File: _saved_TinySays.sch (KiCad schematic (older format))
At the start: 31 parts, among them IC1 ATTINY85-S, P2 USB_OTG, P3 CONN_01X02, SW1 Switch_SPDT_x2, U1 MCP73831

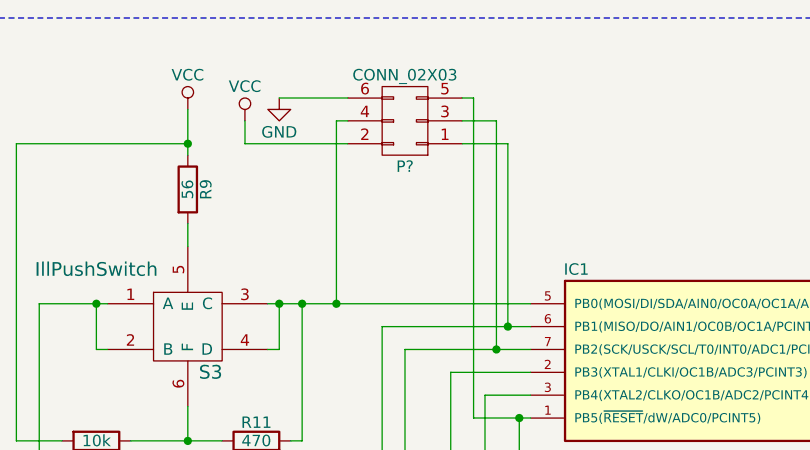
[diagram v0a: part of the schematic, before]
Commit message: PCB v2.0 40mm x 40mm done
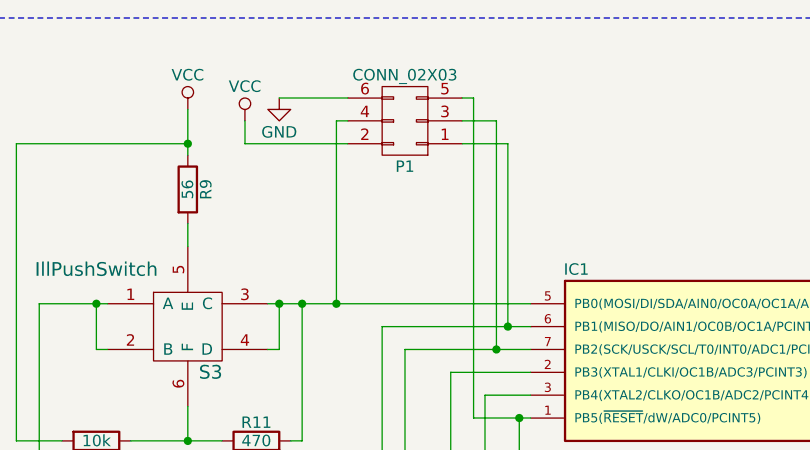
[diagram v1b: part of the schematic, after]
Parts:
- P1: renamed from P?; footprint (none) -> Pin_Headers:Pin_Header_Angled_2x03
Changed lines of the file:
@@
 Connection ~ 1350 6900
 $Comp
-L CONN_02X03 P?
+L CONN_02X03 P1
 U 1 1 5718124E
 P 7650 2150
-F 0 "P?" H 7650 2350 50  0000 C CNN
+F 0 "P1" H 7650 2350 50  0000 C CNN
 F 1 "CONN_02X03" H 7650 1950 50  0000 C CNN
-F 2 "" H 7650 950 50  0000 C CNN
+F 2 "Pin_Headers:Pin_Header_Angled_2x03" H 7650 950 50  0001 C CNN
 F 3 "" H 7650 950 50  0000 C CNN
 	1    7650 2150
@@
 Connection ~ 5250 2950
 $Comp
-L VCC #PWR?
+L VCC #PWR018
 U 1 1 571889FE
 P 6950 2150
-F 0 "#PWR?" H 6950 2000 50  0001 C CNN
+F 0 "#PWR018" H 6950 2000 50  0001 C CNN
 F 1 "VCC" H 6950 2300 50  0000 C CNN
 F 2 "" H 6950 2150 50  0000 C CNN
@@
 $EndComp
 $Comp
-L GND #PWR?
+L GND #PWR019
 U 1 1 57188A66
 P 7100 2050
-F 0 "#PWR?" H 7100 1800 50  0001 C CNN
+F 0 "#PWR019" H 7100 1800 50  0001 C CNN
 F 1 "GND" H 7100 1900 50  0000 C CNN
 F 2 "" H 7100 2050 50  0000 C CNN
